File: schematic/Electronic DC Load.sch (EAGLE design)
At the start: 47 parts, among them Q1 16MHz, Q2 IRFP250, SW1 EC12E_SW, U1 REF5050_D_8, U2 REF192GSZ-REEL, U3 ATMEGA328P_TQFP, U4 AD7190BRUZ-REEL, U5 TLV5616_D_8, U6 LM358-N, U7 AD8629ARZ

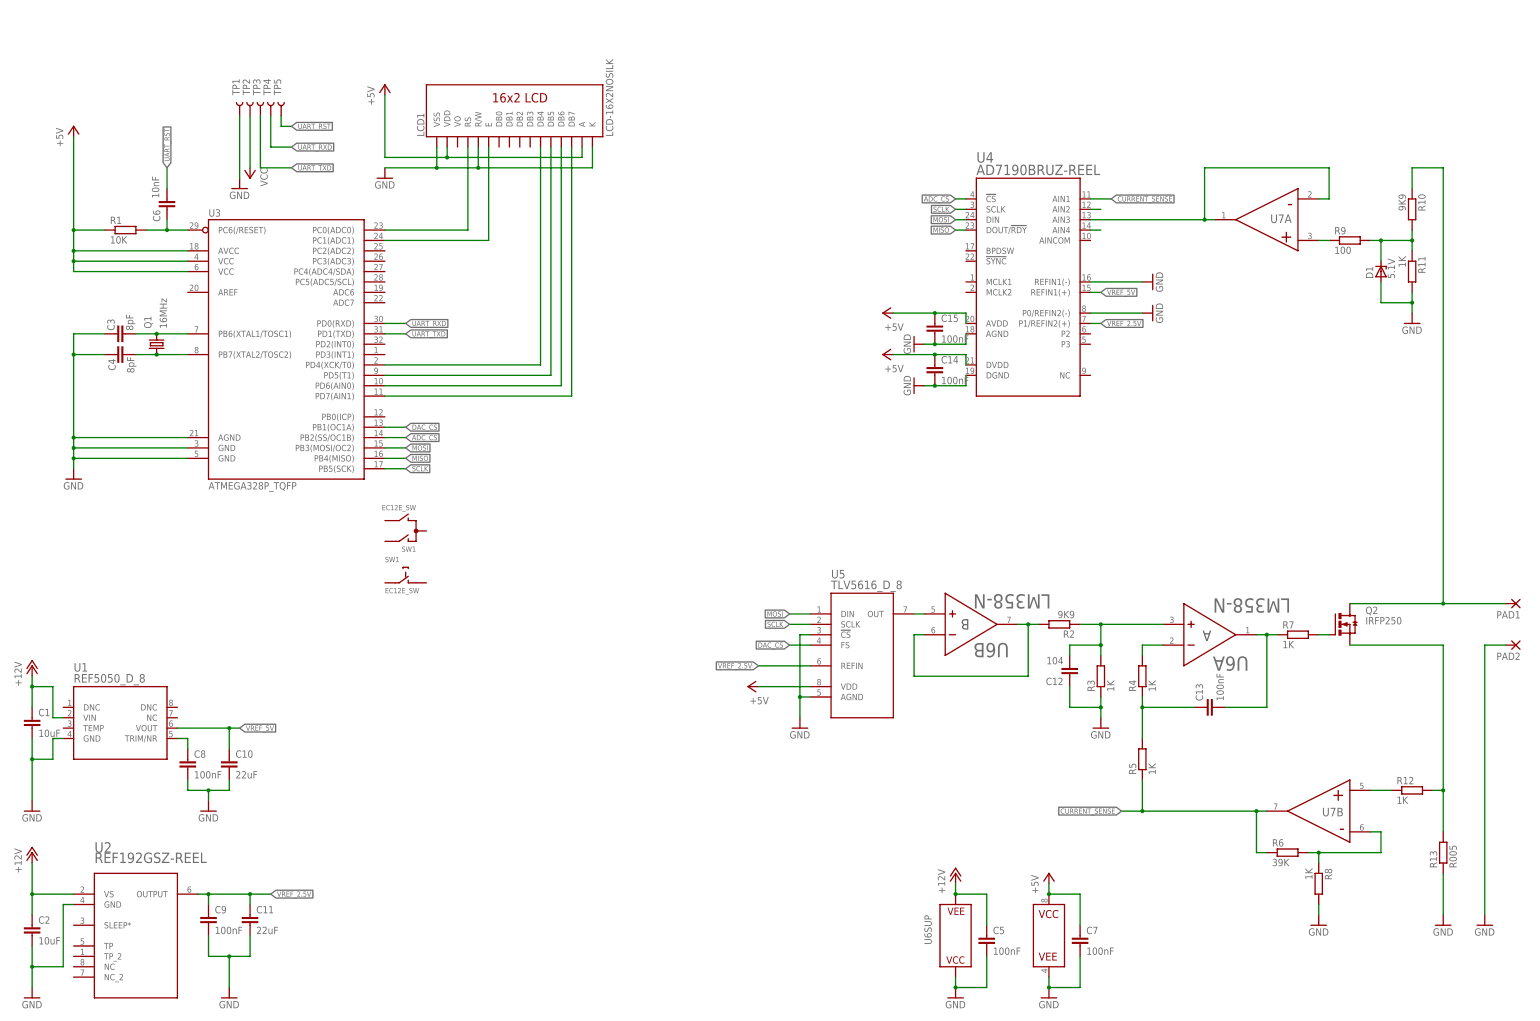
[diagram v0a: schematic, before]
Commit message: Remove the old version of schematics
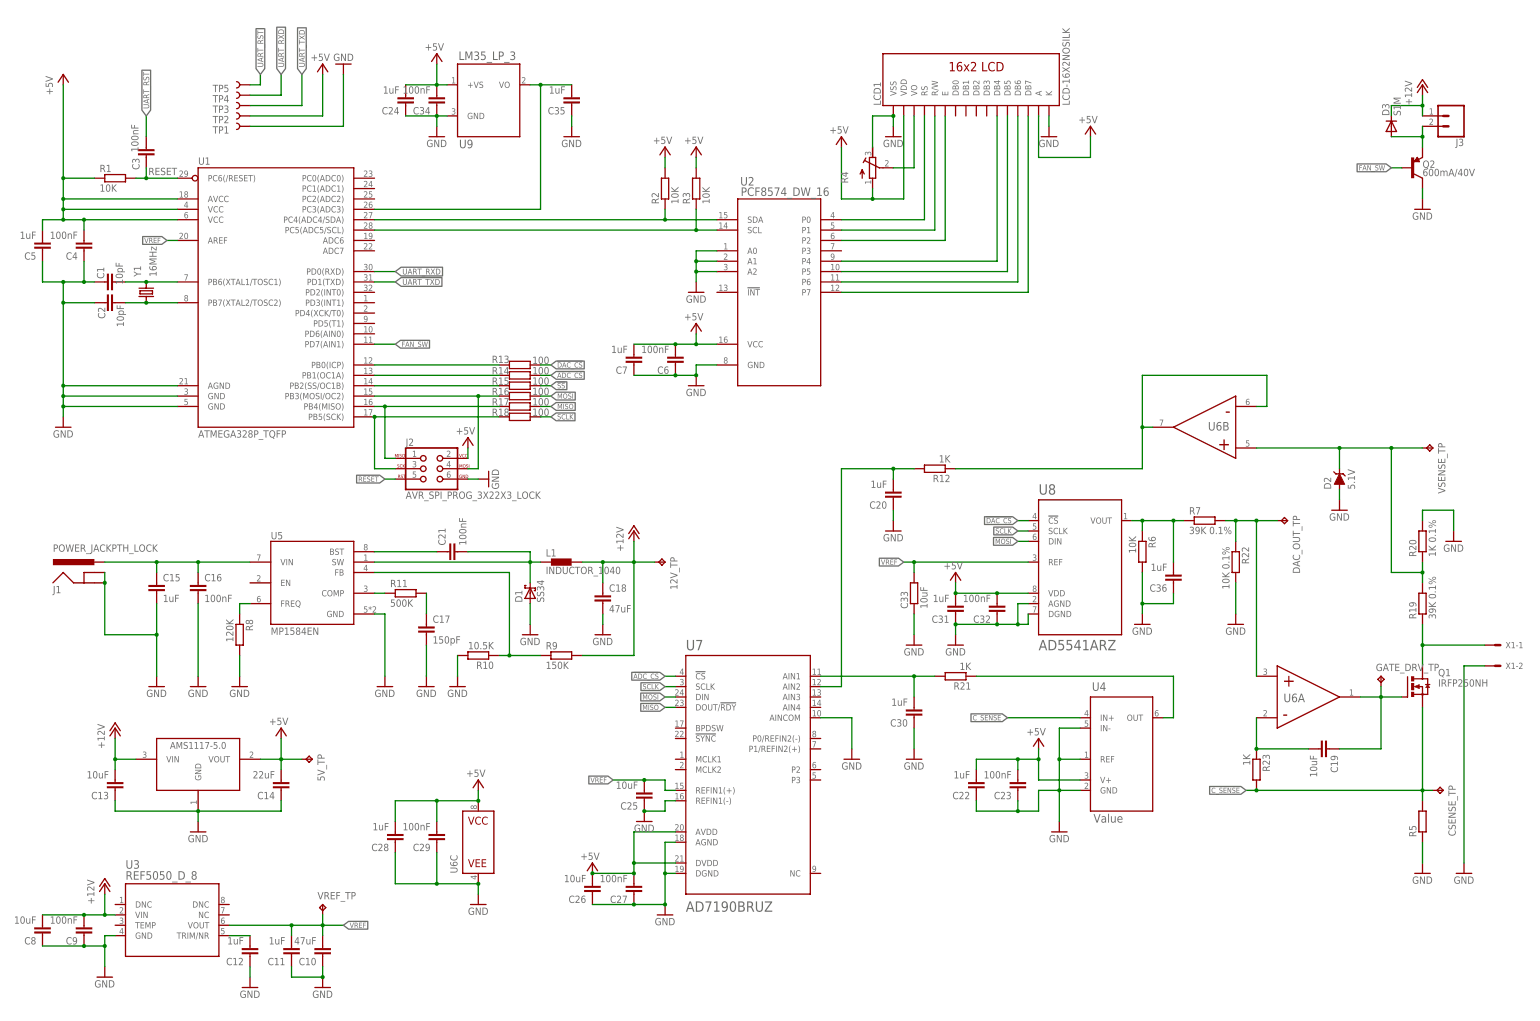
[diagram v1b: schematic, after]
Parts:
- removed PAD1, PAD2: (no value), wirepad:SMD5
- removed SW1: EC12E_SW, alps:EC12E_SW
- added 12V_TP, 5V_TP, CSENSE_TP, DAC_OUT_TP, GATE_DRV_TP, VREF_TP, VSENSE_TP: TPB2,54, testpad:TPB2,54
- added C16, C23, C29: 100nF, resistor:C-EUC0805
- added C17: 150pF, resistor:C-EUC1206
- added C18: 47uF, resistor:C-EUC1206
- added C19, C25, C26: 10uF, resistor:C-EUC0603
- added C20, C22, C28, C30: 1uF, resistor:C-EUC0805
- added C21: 100nF, resistor:C-EUC1206
- added C24, C31, C35, C36: 1uF, resistor:C-EUC0603
- added C27, C32, C34: 100nF, resistor:C-EUC0603
- added C33: 10uF, resistor:R-EU_M1206
- added D2: 5.1V, 0_discrete:DIODE-ZENER-5.1V
- added D3: S1M, diode:S1M
- added J1: POWER_JACKPTH_LOCK, SparkFun-Connectors:POWER_JACKPTH_LOCK
- added J2: AVR_SPI_PROG_3X22X3_LOCK, SparkFun-Connectors:AVR_SPI_PROG_3X22X3_LOCK
- added J3: (no value), SparkFun-Connectors:CONN_02LOCK_LONGPADS
- added L1: INDUCTOR_1040, 0_discrete:INDUCTOR_1040
- added R14, R15, R16, R17, R18: 100, resistor:R-EU_M0805
- added R19: 39K 0.1%, resistor:R-EU_M0805
- added R20: 1K 0.1%, resistor:R-EU_M0805
- added R21, R23: 1K, resistor:R-EU_R0805
- added R22: 10K 0.1%, resistor:R-EU_R0805
- added U$1: AMS1117-5.0, AMS1117-5.0:AMS1117-5.0
- added U8: AD5541ARZ, 0_analog-devices:AD5541ARZ
- added U9: LM35_LP_3, 0_texas-instrument:LM35_LP_3
- added X1: (no value), con-molex:KK-156-2
- added Y1: 16MHz, crystal-geyer_V1_0:KX-7
- C1, C2: value 10uF -> 10pF; device resistor:C-EUC1206 -> resistor:C-EUC0603
- C10: value 22uF -> 47uF; device resistor:C-EUC1206 -> resistor:C-EUC0603
- C11: value 22uF -> 1uF; device resistor:C-EUC1206 -> resistor:C-EUC0603
- C12: value 104 -> 1uF
- C13: value 100nF -> 10uF
- C14: value 100nF -> 22uF
- C15: value 100nF -> 1uF; device resistor:C-EUC0603 -> resistor:C-EUC0805
- C3, C4: value 8pF -> 100nF
- C5, C7: value 100nF -> 1uF; device resistor:C-EUC1206 -> resistor:C-EUC0603
- C6: value 10nF -> 100nF
- C8: value 100nF -> 10uF; device resistor:C-EUC1206 -> resistor:C-EUC0603
- C9: device resistor:C-EUC1206 -> resistor:C-EUC0603
- D1: value 5.1V -> SS34; device diode:ZENER-DIODESOD80C -> diode:SCHOTTKY-DIODESMC
- Q1: value 16MHz -> IRFP250NH; device crystal-geyer_V1_0:KX-7 -> 0_discrete:IRFP250NH
- Q2: value IRFP250 -> 600mA/40V; device transistor-power:IRFP250 -> SparkFun-DiscreteSemi:TRANS_PNP-MMBT4403
- R10: value 9K9 -> 10.5K; device resistor:R-EU_R0805 -> resistor:R-EU_R0603
- R11: value 1K -> 500K; device resistor:R-EU_R0805 -> resistor:R-EU_R0603
- R12: device resistor:R-EU_R0603 -> resistor:R-EU_R0805
- R13: value R005 -> 100; device resistor:R-EU_R2512 -> resistor:R-EU_M0805
- R2: value 9K9 -> 10K
- R3: value 1K -> 10K
- R4: value 1K -> (none); device resistor:R-EU_R0603 -> resistor:R-TRIMM3296P
- R5: value 1K -> (none); device resistor:R-EU_R0603 -> 0_sup:MRE_R005_4W_2728_1%
- R6: value 39K -> 10K; device resistor:R-EU_M0805 -> resistor:R-EU_R0805
- R7: value 1K -> 39K 0.1%; device resistor:R-EU_R0603 -> resistor:R-EU_R0805
- R8: value 1K -> 120K; device resistor:R-EU_R0805 -> resistor:R-EU_R0603
- R9: value 100 -> 150K; device resistor:R-EU_R0805 -> resistor:R-EU_R0603
- U1: value REF5050_D_8 -> ATMEGA328P_TQFP; device texas_instrument:REF5050_D_8 -> SparkFun-IC-Microcontroller:ATMEGA328P_TQFP
- U2: value REF192GSZ-REEL -> PCF8574_DW_16; device analog_devices:REF192GSZ-REEL -> 0_texas-instrument:PCF8574_DW_16
- U3: value ATMEGA328P_TQFP -> REF5050_D_8; device SparkFun-IC-Microcontroller:ATMEGA328P_TQFP -> 0_texas-instrument:REF5050_D_8
- U4: value AD7190BRUZ-REEL -> Value; device analog_devices:AD7190BRUZ-REEL -> 0_texas-instrument:INA210AIDCKRG4
- U5: value TLV5616_D_8 -> MP1584EN; device texas_instrument:TLV5616_D_8 -> MP1584EN:MP1584EN
- U6: value LM358-N -> AD8629ARZ; device texas_instrument:LM358-N -> 0_analog-devices:AD8629ARZ
- U7: value AD8629ARZ -> AD7190BRUZ; device analog_devices:AD8629ARZ -> 0_analog-devices:AD7190BRUZ
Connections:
- removed net ADC_CS: U3.PB2(SS/OC1B), U4.!CS
- removed net CURRENT_SENSE: R5.1, R6.1, U4.AIN1, U7B.OUT
- removed net DAC_CS: U3.PB1(OC1A), U5.FS
- removed net VREF_2.5V: C11.1, C9.1, U2.OUTPUT, U4.P1/REFIN2(+), U5.REFIN
- removed net VREF_5V: C10.1, U1.VOUT, U4.REFIN1(+)
- new net !ADC_CS: R14.2, U7.!CS
- new net !DAC_CS: R13.2, U8.!CS
- new net !SS: R15.2
- new net C_SENSE: CSENSE_TP.TP, Q1.S, R23.2, R5.2, U4.IN+
- new net FAN_SW: Q2.B, U1.PD7(AIN1)
- new net N$23: R11.1, U5.COMP
- new net N$25: C17.1, R11.2
- new net N$27: R12.1, U6B.IN-, U6B.OUT
- new net N$30: J2.3, R18.1, U1.PB5(SCK)
- new net N$31: J2.1, R17.1, U1.PB4(MISO)
- new net N$32: J2.4, R16.1, U1.PB3(MOSI/OC2)
- new net N$33: R15.1, U1.PB2(SS/OC1B)
- new net N$34: R14.1, U1.PB1(OC1A)
- new net N$35: R13.1, U1.PB0(ICP)
- new net N$36: C19.1, GATE_DRV_TP.TP, Q1.G, U6A.OUT
- new net N$37: D2.C, R19.2, R20.1, U6B.IN+, VSENSE_TP.TP
- new net N$39: DAC_OUT_TP.TP, R22.1, R7.2, U6A.IN+
- new net RESET: C3.1, J2.5, R1.2, U1.PC6(/RESET)
- new net VREF: C10.2, C11.2, C25.2, C33.2, U1.AREF, U3.VOUT, U7.REFIN1(+), U8.REF, VREF_TP.TP
- net +12V: now also 12V_TP.TP, C13.2, C18.1, C8.2, C9.2, D3.C, J3.1, L1.2, R9.2, U$1.VIN, U3.VIN; no longer C5.1, U6SUP.VEE
- net +5V: now also 5V_TP.TP, C14.2, C22.2, C23.2, C24.2, C26.2, C27.2, C28.2, C29.2, C31.2, C32.2, C34.2, C6.2, C7.2, J2.2, LCD1.A, LCD1.VDD, R2.2, R3.2, R4.A, U$1.VOUT, U2.VCC, U4.V+, U6C.VCC, U7.AVDD, U7.DVDD, U8.VDD, U9.+VS; no longer C14.1, C15.1, U4.AVDD, U4.DVDD, U5.VDD
- net GND: now also C1.1, C10.1, C11.1, C13.1, C14.1, C16.2, C17.2, C18.2, C2.1, C20.1, C22.1, C23.1, C24.1, C25.1, C26.1, C27.1, C28.1, C29.1, C30.1, C31.1, C32.1, C33.1, C34.1, C35.1, C36.1, C5.1, C6.1, C7.1, C8.1, C9.1, D2.A, J1.GND, J1.GNDBREAK, J2.6, Q2.C, R10.2, R20.2, R22.2, R4.E, R5.1, R6.2, U$1.GND, U1.AGND, U1.GND@3, U1.GND@5, U2.A0, U2.A1, U2.A2, U3.GND, U4.GND, U4.IN-, U4.REF, U5.GND, U6C.VEE, U7.AGND, U7.AINCOM, U7.DGND, U7.REFIN1(-), U8.AGND, U8.DGND, U9.GND, X1-2.S; no longer C1.2, C10.2, C11.2, C14.2, C2.2, C3.1, C5.2, C7.2, C8.2, C9.2, LCD1.R/W, PAD2.P, R11.2, R13.1, R3.1, U1.GND, U3.AGND, U3.GND@3, U3.GND@5, U4.AGND, U4.DGND, U4.P0/REFIN2(-), U4.REFIN1(-), U5.!CS, U5.AGND, U6SUP.VCC, U7C.VEE
- net MISO: now also R17.2, U7.DOUT/!RDY; no longer U3.PB4(MISO), U4.DOUT/!RDY
- net MOSI: now also R16.2, U7.DIN, U8.DIN; no longer U3.PB3(MOSI/OC2), U4.DIN, U5.DIN
- net N$1: now also R2.1, U1.PC4(ADC4/SDA), U2.SDA; no longer Q2.S, R12.2, R13.2
- net N$10: now also C12.2, U3.TRIM/NR; no longer D1.C, R10.2, R11.1, R9.2
- net N$11: now also C1.2, U1.PB6(XTAL1/TOSC1), Y1.2; no longer C3.2, Q1.2, U3.PB6(XTAL1/TOSC1)
- net N$12: now also C2.2, U1.PB7(XTAL2/TOSC2), Y1.1; no longer C4.2, Q1.1, U3.PB7(XTAL2/TOSC2)
- net N$13: now also LCD1.VO, R4.S; no longer C12.2, R2.1, R3.2, U6A.IN+
- net N$14: now also Q1.D, R19.1, X1-1.S; no longer R9.1, U7A.IN+
- net N$15: now also C35.2, U1.PC3(ADC3), U9.VO; no longer C6.1, R1.2, U3.PC6(/RESET)
- net N$16: now also C20.2, R12.2, U7.AIN2; no longer U4.AIN4
- net N$17: now also R8.1, U5.FREQ; no longer LCD1.DB4, U3.PD4(XCK/T0)
- net N$18: now also R21.1, U4.OUT; no longer LCD1.DB5, U3.PD5(T1)
- net N$19: now also C21.1, U5.BST; no longer LCD1.DB6, U3.PD6(AIN0)
- net N$2: now also R3.1, U1.PC5(ADC5/SCL), U2.SCL; no longer C13.1, R4.1, R5.2
- net N$20: now also C15.1, C16.1, J1.PWR, U5.VIN; no longer LCD1.DB7, U3.PD7(AIN1)
- net N$21: now also C21.2, D1.C, L1.1, U5.SW; no longer LCD1.RS, U3.PC0(ADC0)
- net N$22: now also R10.1, R9.1, U5.FB; no longer LCD1.E, U3.PC1(ADC1)
- net N$24: now also C30.2, R21.2, U7.AIN1; no longer C13.2, R7.1, U6A.OUT
- net N$26: now also C36.2, R6.1, R7.1, U8.VOUT; no longer R4.2, U6A.IN-
- net N$28: now also D3.A, J3.2, Q2.E; no longer R2.2, U6B.IN-, U6B.OUT
- net N$29: now also C19.2, R23.1, U6A.IN-; no longer U5.OUT, U6B.IN+
- net N$3: now also LCD1.DB4, U2.P4; no longer U4.AIN2
- net N$4: now also LCD1.DB5, U2.P5; no longer R6.2, R8.1, U7B.IN-
- net N$5: now also LCD1.DB6, U2.P6; no longer C8.1, U1.TRIM/NR
- net N$6: now also LCD1.DB7, U2.P7; no longer R12.1, U7B.IN+
- net N$7: now also LCD1.RS, U2.P0; no longer Q2.G, R7.2
- net N$8: now also LCD1.R/W, U2.P1; no longer U4.AIN3, U7A.IN-, U7A.OUT
- net N$9: now also LCD1.E, U2.P2; no longer PAD1.P, Q2.D, R10.1
- net SCLK: now also R18.2, U7.SCLK, U8.SCLK; no longer U3.PB5(SCK), U4.SCLK, U5.SCLK
- net UART_RST: now also C3.2; no longer C6.2
- net UART_RXD: now also U1.PD0(RXD); no longer U3.PD0(RXD)
- net UART_TXD: now also U1.PD1(TXD); no longer U3.PD1(TXD)
- net VCC: now also C4.2, C5.2, U1.AVCC, U1.VCC@4, U1.VCC@6; no longer C1.1, C2.1, C7.1, LCD1.A, LCD1.VDD, U1.VIN, U2.VS, U3.AVCC, U3.VCC@4, U3.VCC@6, U7C.VCC
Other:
- moved on the sheet: C1, C10, C11, C12, C13, C14, C15, C2, C3, C4, C5, C6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

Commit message: Update components
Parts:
- U4: value Value -> INA210AIDCKRG4
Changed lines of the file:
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@@
 <part name="R5" library="0_sup" deviceset="MRE_R005_4W_2728_1%" device=""/>
 <part name="GND11" library="supply1" library_urn="urn:adsk.eagle:library:371" deviceset="GND" device=""/>
-<part name="U4" library="0_texas-instrument" deviceset="INA210AIDCKRG4" device="" value="Value"/>
+<part name="U4" library="0_texas-instrument" deviceset="INA210AIDCKRG4" device="" value="INA210AIDCKRG4"/>
 <part name="GND12" library="supply1" library_urn="urn:adsk.eagle:library:371" deviceset="GND" device=""/>
 <part name="U5" library="MP1584EN" deviceset="MP1584EN" device=""/>

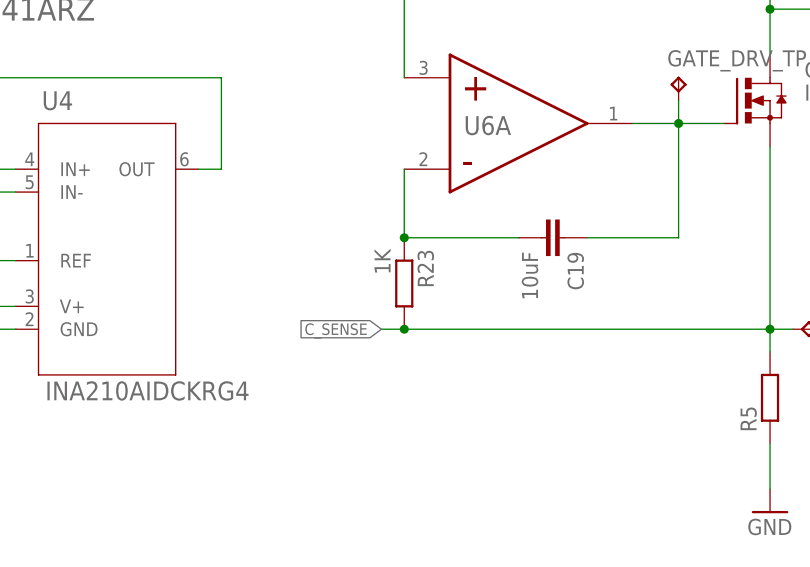
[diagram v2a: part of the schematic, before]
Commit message: Remove the resistor from the input pin of AD8293
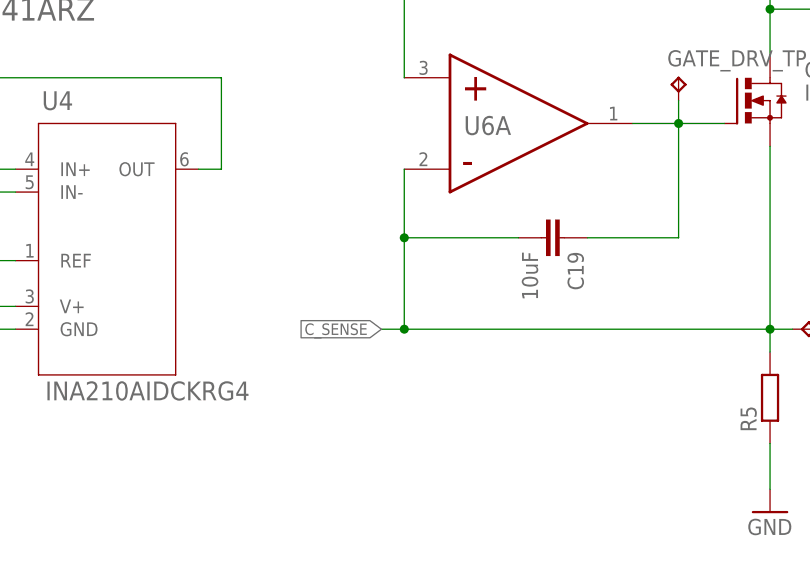
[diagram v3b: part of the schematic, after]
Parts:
- removed R23: 1K, resistor:R-EU_R0805
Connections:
- removed net N$29: C19.2, R23.1, U6A.IN-
- net C_SENSE: now also C19.2, U6A.IN-; no longer R23.2
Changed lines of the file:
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@@
 <part name="R7" library="resistor" library_urn="urn:adsk.eagle:library:348" deviceset="R-EU_" device="R0805" package3d_urn="urn:adsk.eagle:package:26059/1" value="39K 0.1%"/>
 <part name="R22" library="resistor" library_urn="urn:adsk.eagle:library:348" deviceset="R-EU_" device="R0805" package3d_urn="urn:adsk.eagle:package:26059/1" value="10K 0.1%"/>
-<part name="R23" library="resistor" library_urn="urn:adsk.eagle:library:348" deviceset="R-EU_" device="R0805" package3d_urn="urn:adsk.eagle:package:26059/1" value="1K"/>
 <part name="GND37" library="supply1" library_urn="urn:adsk.eagle:library:371" deviceset="GND" device=""/>
 <part name="L1" library="0_discrete" deviceset="INDUCTOR_1040" device=""/>
@@
 <instance part="R7" gate="G$1" x="299.72" y="129.54"/>
 <instance part="R22" gate="G$1" x="307.34" y="119.38" rot="R270"/>
-<instance part="R23" gate="G$1" x="312.42" y="68.58" rot="R270"/>
 <instance part="GND37" gate="1" x="307.34" y="104.14"/>
 <instance part="L1" gate="A" x="142.24" y="119.38"/>
@@
 <wire x1="312.42" y1="63.5" x2="309.88" y2="63.5" width="0.1524" layer="91"/>
 <wire x1="353.06" y1="63.5" x2="355.6" y2="63.5" width="0.1524" layer="91"/>
-<pinref part="R23" gate="G$1" pin="2"/>
+<pinref part="U6" gate="A" pin="IN-"/>
+<wire x1="312.42" y1="81.28" x2="312.42" y2="73.66" width="0.1524" layer="91"/>
+<pinref part="C19" gate="G$1" pin="2"/>
+<wire x1="325.12" y1="73.66" x2="312.42" y2="73.66" width="0.1524" layer="91"/>
+<wire x1="312.42" y1="73.66" x2="312.42" y2="63.5" width="0.1524" layer="91"/>
+<junction x="312.42" y="73.66"/>
 <junction x="312.42" y="63.5"/>
 </segment>
@@
 </segment>
 </net>
-<net name="N$29" class="0">
-<segment>
-<pinref part="U6" gate="A" pin="IN-"/>
-<wire x1="312.42" y1="81.28" x2="312.42" y2="73.66" width="0.1524" layer="91"/>
-<pinref part="C19" gate="G$1" pin="2"/>
-<wire x1="325.12" y1="73.66" x2="312.42" y2="73.66" width="0.1524" layer="91"/>
-<pinref part="R23" gate="G$1" pin="1"/>
-<junction x="312.42" y="73.66"/>
-</segment>
-</net>
